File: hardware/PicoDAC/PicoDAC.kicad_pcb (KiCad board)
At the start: 4 copper layers, 29.9 x 82.1 mm, 42 parts, among them CN1 PJ-327A 5JJ, U1 CS43131-CNZR, U2 XIAO-RP2350-DIP, U3 PCA9306DCUR, U4 SN74AXC4T245PWR, U5 XTPS7A2018, U6 TYPEC-955-ARP24, U7 74AHCT1G125GV

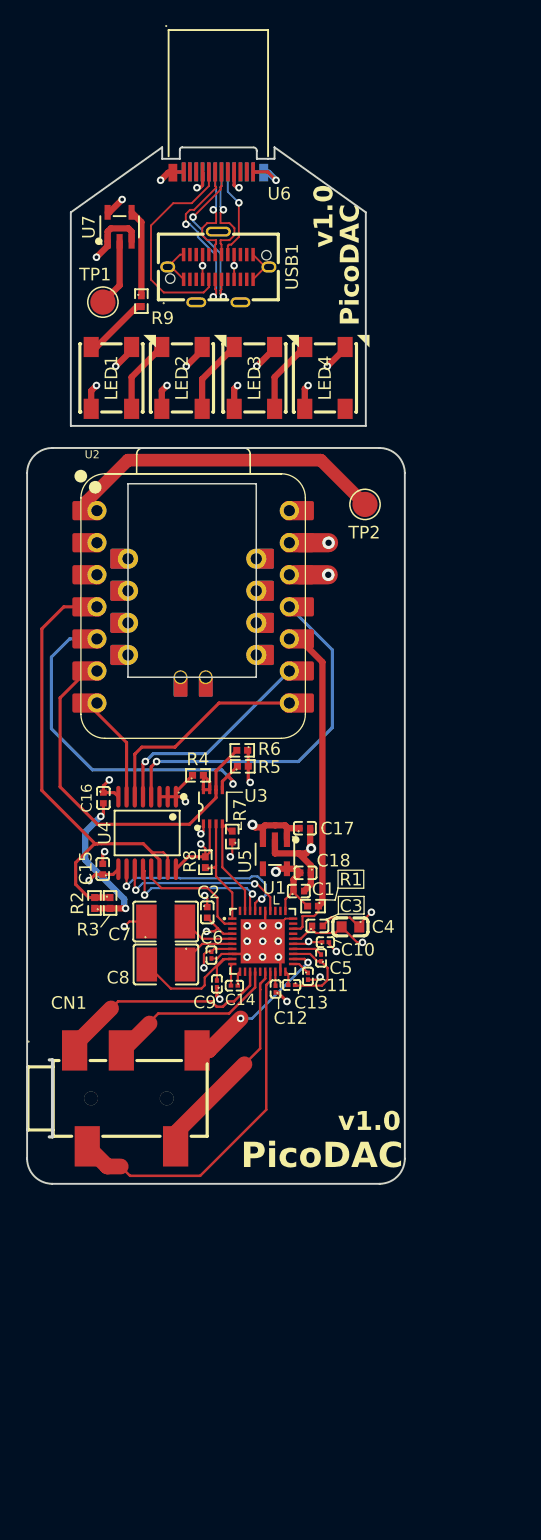
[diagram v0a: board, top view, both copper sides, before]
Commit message: update LEDs position, misc changes to PCBs
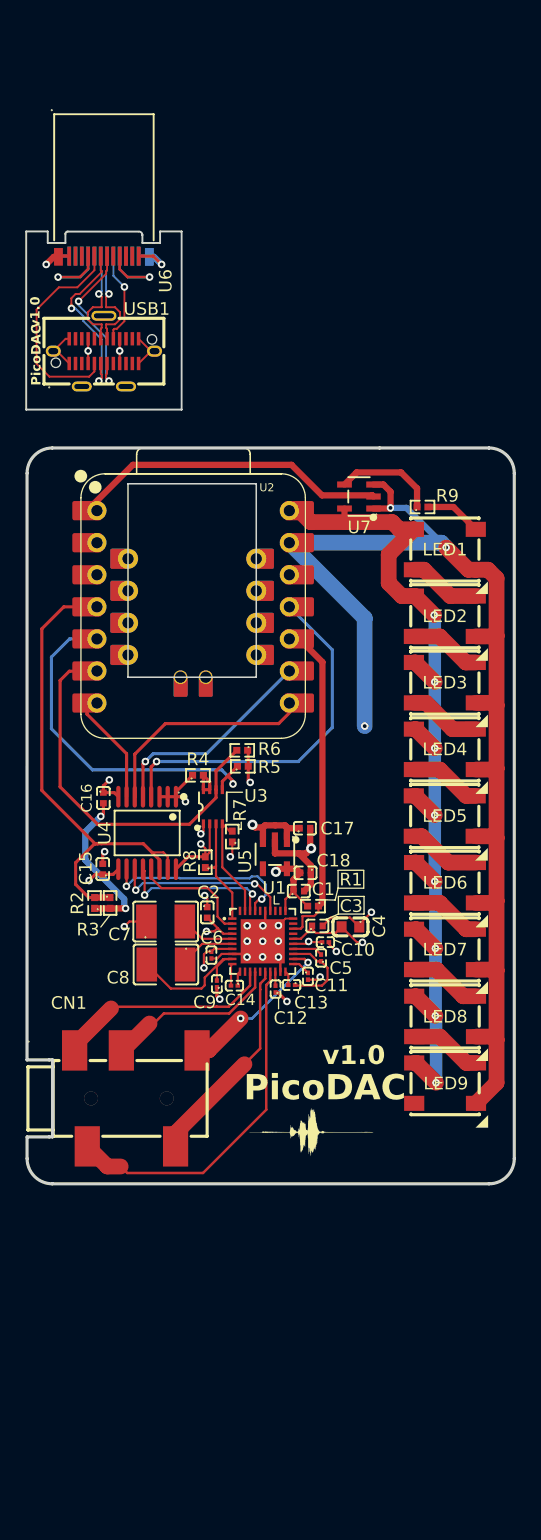
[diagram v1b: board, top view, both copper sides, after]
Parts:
- removed TP1, TP2: TestPoint, TestPoint:TestPoint_Pad_D2.0mm
- added G***: LOGO, LOGO, F.Cu at (153.3, 131.3)
- added LED5: SK6812_C5378720, easyeda2kicad:LED-SMD_4P-L5.4-W5.0_SK6812, F.Cu at (163.9, 106.3)
- added LED6: SK6812_C5378720, easyeda2kicad:LED-SMD_4P-L5.4-W5.0_SK6812, F.Cu at (163.9, 111.6)
- added LED7: SK6812_C5378720, easyeda2kicad:LED-SMD_4P-L5.4-W5.0_SK6812, F.Cu at (163.9, 116.8)
- added LED8: SK6812_C5378720, easyeda2kicad:LED-SMD_4P-L5.4-W5.0_SK6812, F.Cu at (163.9, 122.1)
- added LED9: SK6812_C5378720, easyeda2kicad:LED-SMD_4P-L5.4-W5.0_SK6812, F.Cu at (163.9, 127.4)
- moved LED4 30.9 mm to (163.9, 101.0), turned to 0 degrees
- moved LED1 29.7 mm to (163.9, 85.2), turned to 0 degrees
- moved U7 28.6 mm to (157.1, 81.0), turned to 90 degrees
- moved LED3 28.5 mm to (163.9, 95.7), turned to 0 degrees
- moved LED2 28.1 mm to (163.9, 90.4), turned to 0 degrees
- moved R9 27.6 mm to (162.1, 81.8), turned to 0 degrees
- moved U6 11.3 mm to (136.9, 61.9)
- moved USB1 11.3 mm to (136.9, 69.4)
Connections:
- LED1 pad 1: /USB_GND -> GND
- LED1 pad 3: /USB_VBUS -> VBUS
- LED2 pad 1: /USB_GND -> GND
- LED2 pad 3: /USB_VBUS -> VBUS
- LED3 pad 1: /USB_GND -> GND
- LED3 pad 3: /USB_VBUS -> VBUS
- LED4 pad 1: /USB_GND -> GND
- LED4 pad 3: /USB_VBUS -> VBUS
- LED4 pad 4: unconnected-(LED4-DOUT-Pad4) -> Net-(LED4-DOUT)
- U2 pad 1: /MCU_GP_26 -> /LED_CONTROL
- U7 pad 1: /USB_GND -> GND
- U7 pad 3: /USB_GND -> GND
- U7 pad 5: /USB_VBUS -> VBUS
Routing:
- net GND: track 50.0 -> 146.4 mm, vias 20 -> 22
- net /USB_VBUS: track 102.4 -> 18.6 mm, vias 9 -> 4
- net VBUS: track 0.00 -> 73.8 mm, vias 0 -> 8
- net /MCU_GP_26: track 25.6 -> 0.00 mm
- net /LED_CONTROL: track 5.36 -> 25.3 mm
- net /USB_GND: track 28.4 -> 14.8 mm, vias 7 -> 2
- net Net-(LED7-DOUT): track 0.00 -> 5.78 mm
- net Net-(LED5-DOUT): track 0.00 -> 5.78 mm
- net Net-(LED8-DOUT): track 0.00 -> 5.76 mm
- net Net-(LED6-DOUT): track 0.00 -> 5.76 mm
- net Net-(LED4-DOUT): track 0.00 -> 5.75 mm
- net Net-(U7-Y): track 6.92 -> 8.14 mm
- net /MCU_GP_07: track 29.0 -> 29.8 mm
- net Net-(LED1-DIN): track 5.30 -> 4.52 mm
- net +3.3V: track 88.5 -> 88.8 mm, vias 7 -> 6
- added copper zone on In2.Cu, net /USB_VBUS
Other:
- board size 29.9 x 82.1 mm -> 38.7 x 75.4 mm

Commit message: moved the LEDs a bit down, repositioned LEDs logic level translator and resistor
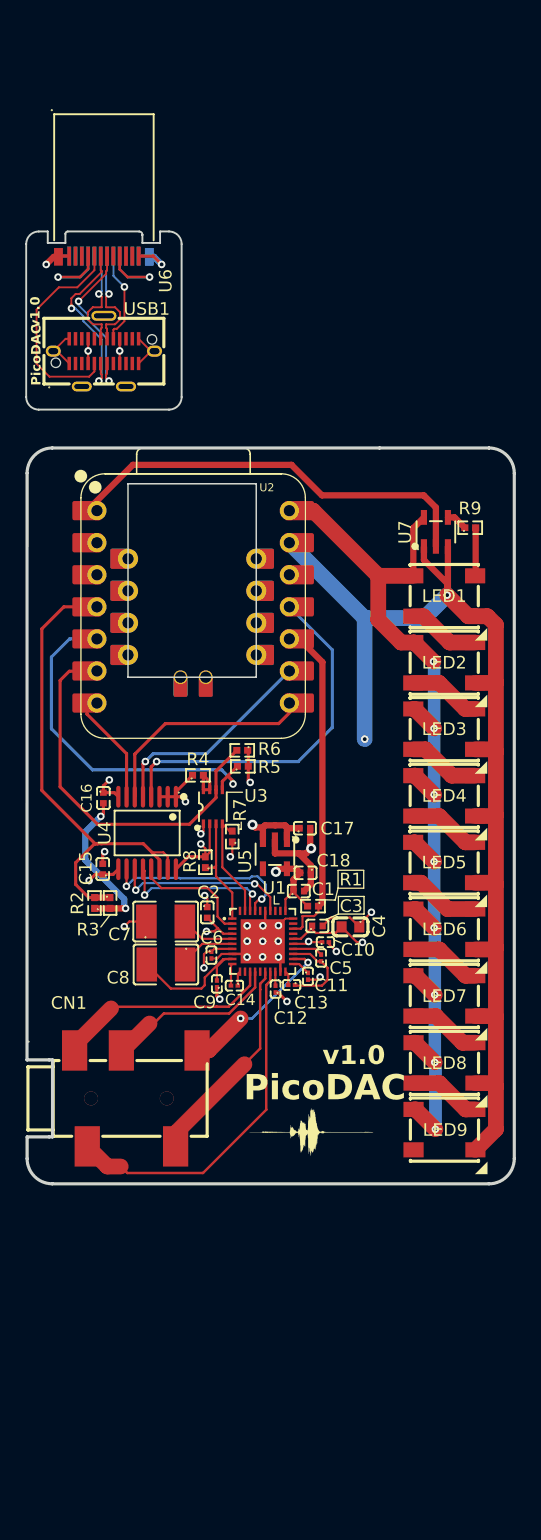
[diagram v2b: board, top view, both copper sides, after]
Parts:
- moved U7 6.71 mm to (163.2, 83.8), turned to 0 degrees
- moved R9 4.12 mm to (165.9, 83.4)
- moved LED1 3.68 mm to (163.8, 88.8)
- moved LED2 3.68 mm to (163.8, 94.1)
- moved LED3 3.68 mm to (163.8, 99.4)
- moved LED4 3.68 mm to (163.8, 104.7)
- moved LED5 3.68 mm to (163.8, 110.0)
- moved LED6 3.68 mm to (163.9, 115.2)
- moved LED7 3.68 mm to (163.9, 120.5)
- moved LED8 3.68 mm to (163.9, 125.8)
- moved LED9 3.68 mm to (163.9, 131.1)
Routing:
- net /LED_CONTROL: track 25.3 -> 33.7 mm
- net Net-(U7-Y): track 8.14 -> 1.68 mm
- net GND: track 146.4 -> 140.5 mm, vias 22 -> 21
- net VBUS: track 73.8 -> 78.6 mm
- net Net-(LED1-DIN): track 4.52 -> 3.83 mm
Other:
- outline, holes or cut-outs redrawn

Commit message: final pcb, rev 1.2
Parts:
- added REF**: MouseBite-Slot_2.0x2.0mm_outset_D0.5mm_P0.85mm_3h, Panelization:MouseBite-Slot_2.0x2.0mm_outset_D0.5mm_P0.85mm_3h, F.Cu at (155.7, 137.4)
- added REF**: MouseBite-Slot_2.0x2.0mm_outset_D0.5mm_P0.85mm_3h, Panelization:MouseBite-Slot_2.0x2.0mm_outset_D0.5mm_P0.85mm_3h, F.Cu at (149.8, 137.4)
- moved U6 89.0 mm to (152.8, 149.6), turned to 0 degrees
- moved USB1 74.3 mm to (152.8, 142.1), turned to 0 degrees
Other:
- board size 38.7 x 75.4 mm -> 38.6 x 74.4 mm

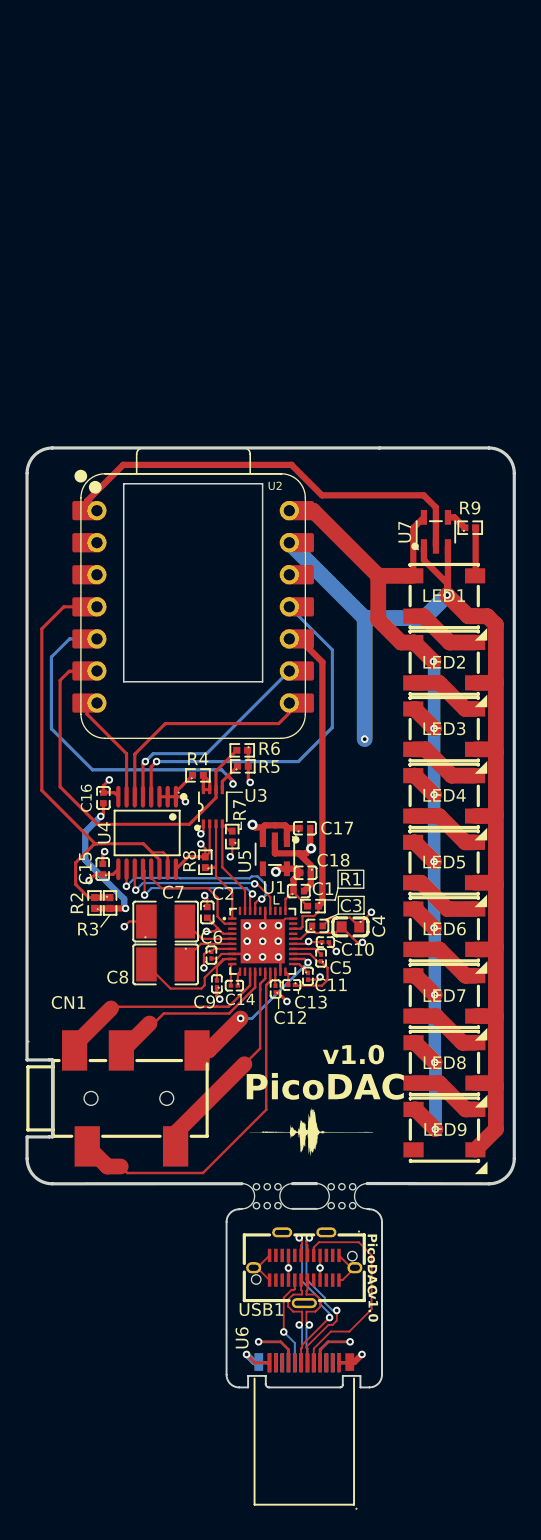
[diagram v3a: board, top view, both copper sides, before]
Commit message: changed components to get economic assembly
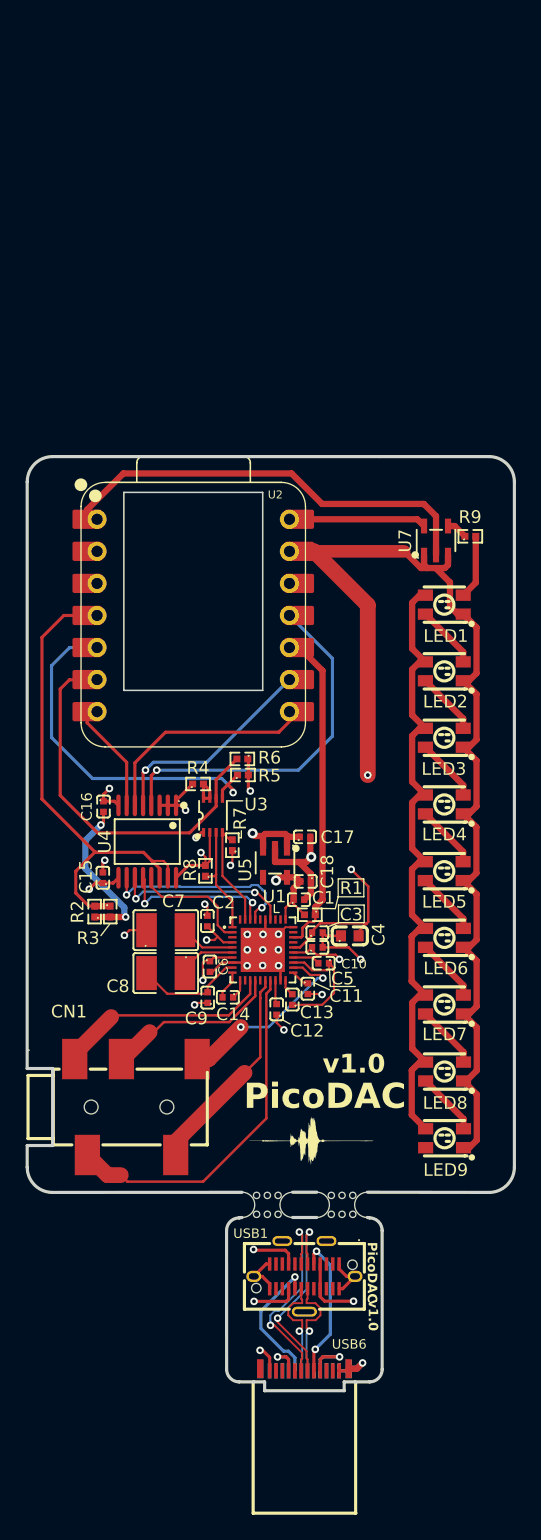
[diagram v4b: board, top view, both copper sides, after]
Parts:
- removed U6: TYPEC-955-ARP24, easyeda2kicad:USB-C-SMD_TYPE-C-24P-GTJB-040
- added USB6: XY-TYPE-C-24PIN-040, easyeda2kicad:USB-C-SMD_XY-TYPE-C-24PIN-040, F.Cu at (152.8, 150.1)
- C10, C11, C12, C13, C14, C5, C6, C9: footprint easyeda2kicad:C0201 -> easyeda2kicad:C0402
- LED1, LED2, LED3, LED4, LED5, LED6, LED7, LED8, LED9: value SK6812_C5378720 -> SK6812_C5142047; footprint easyeda2kicad:LED-SMD_4P-L5.4-W5.0_SK6812 -> easyeda2kicad:LED-SMD_4P-L3.5-W2.8-BR-1
- moved C12 1.61 mm to (150.6, 121.6)
- moved C9 1.30 mm to (145.1, 120.7)
- moved C13 1.15 mm to (151.8, 120.8), turned to 90 degrees
- moved C14 1.06 mm to (146.7, 120.6)
- moved C11 0.99 mm to (153.0, 120.0)
- moved C6 0.92 mm to (145.3, 118.2)
- moved C10 0.76 mm to (153.8, 116.7)
- moved R1 0.73 mm to (153.2, 114.1)
- moved C4 0.72 mm to (156.4, 115.8), turned to 0 degrees
- moved C1 0.68 mm to (152.3, 112.9)
- moved C15 0.68 mm to (136.8, 111.2)
- moved C18 0.68 mm to (152.9, 111.5)
- moved C2 0.68 mm to (145.1, 114.6)
- moved C7 0.68 mm to (141.8, 115.3)
- moved C8 0.68 mm to (141.8, 118.7)
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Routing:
- net VBUS: track 78.6 -> 61.5 mm, vias 8 -> 0
- net /USB_CC1: track 17.1 -> 11.6 mm, vias 0 -> 2
- net /USB_CC2: track 7.39 -> 10.8 mm
- net /USB_VBUS: track 18.6 -> 21.5 mm, vias 4 -> 5
- net /USB_DN1: track 13.3 -> 16.2 mm
- net Net-(U1-FLYC_VCP): track 6.92 -> 9.80 mm
- net Net-(U1--VA): track 11.5 -> 8.63 mm
- net /DAC_HP_DETECT: track 13.7 -> 16.0 mm
- net +1V8: track 34.4 -> 36.7 mm
- net /USB_DP1: track 13.9 -> 15.7 mm
- net +3.3V: track 88.8 -> 90.6 mm
- net /USB_GND: track 14.8 -> 13.4 mm
- net Net-(LED1-DIN): track 3.83 -> 5.07 mm
- net GND: track 140.5 -> 139.4 mm, vias 21 -> 19
- net Net-(U1-VCP_FILT–): track 1.11 -> 1.92 mm
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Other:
- board size 38.6 x 74.4 mm -> 38.6 x 73.3 mm

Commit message: pcb rev 1.4
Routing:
- net GND: track 139.4 -> 130.0 mm
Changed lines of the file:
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@@
 	)
 	(gr_line
+		(start 154.6684 116.676)
+		(end 156.09 116.69)
+		(stroke
+			(width 0.1)
+			(type default)
+		)
+		(layer "F.SilkS")
+	)
+	(gr_line
+		(start 156.09 116.69)
+		(end 156.61 117.36)
+		(stroke
+			(width 0.1)
+			(type default)
+		)
+		(layer "F.SilkS")
+	)
+	(gr_line
 		(start 150.395147 113.2806)
 		(end 150.395147 113.9156)
@@
 	)
 	(segment
-		(start 144.2312 121.0744)
-		(end 144.0728 121.2328)
-		(width 0.175)
+		(start 155.6696 115.8696)
+		(end 156.74 116.94)
+		(width 0.5)
 		(layer "F.Cu")
 		(net 27)
 	)
 	(segment
-		(start 156.279387 116.676)
-		(end 157.229581 117.626194)
-		(width 0.2)
+		(start 144.2312 121.0744)
+		(end 144.0728 121.2328)
+		(width 0.175)
 		(layer "F.Cu")
 		(net 27)
@@
 	)
 	(segment
-		(start 151.279397 115.0786)
-		(end 149.479397 116.8786)
-		(width 0.15)
+		(start 149.679397 114.4686)
+		(end 149.679397 116.6786)
+		(width 0.2)
 		(layer "F.Cu")
 		(net 27)
@@
 	)
 	(segment
-		(start 149.479397 116.8786)
-		(end 149.479397 116.87825)
-		(width 0.15)
+		(start 151.267897 115.0901)
+		(end 149.479397 116.8786)
+		(width 0.175)
 		(layer "F.Cu")
 		(net 27)
@@
 	)
 	(segment
-		(start 149.479397 116.87825)
-		(end 148.249947 115.6488)
-		(width 0.15)
-		(layer "F.Cu")
-		(net 27)
-	)
-	(segment
 		(start 166.419 112.459)
 		(end 165.3492 111.3892)
@@
 	)
 	(segment
-		(start 148.260547 116.8786)
-		(end 148.249947 116.868)
-		(width 0.15)
-		(layer "F.Cu")
-		(net 27)
-	)
-	(segment
 		(start 165.358 100.821643)
 		(end 165.81 100.821643)
@@
 	)
 	(segment
-		(start 151.889397 115.0786)
-		(end 151.279397 115.0786)
-		(width 0.15)
+		(start 148.479397 117.8786)
+		(end 149.479397 116.8786)
+		(width 0.2)
 		(layer "F.Cu")
 		(net 27)
@@
 	)
 	(segment
-		(start 145.492403 118.6168)
-		(end 146.230603 117.8786)
+		(start 151.889397 115.0786)
+		(end 151.877897 115.0901)
 		(width 0.175)
 		(layer "F.Cu")
@@
 	)
 	(segment
-		(start 148.479397 117.8786)
-		(end 149.479397 116.8786)
-		(width 0.2)
-		(layer "F.Cu")
-		(net 27)
-	)
-	(segment
-		(start 149.479397 116.8786)
-		(end 149.479397 115.66395)
-		(width 0.15)
-		(layer "F.Cu")
-		(net 27)
-	)
-	(segment
-		(start 145.2888 118.6168)
-		(end 145.492403 118.6168)
-		(width 0.175)
+		(start 155.6696 115.7672)
+		(end 155.6696 115.8696)
+		(width 0.5)
 		(layer "F.Cu")
 		(net 27)
@@
 	)
 	(segment
-		(start 147.069397 117.8786)
-		(end 148.479397 117.8786)
-		(width 0.2)
-		(layer "F.Cu")
-		(net 27)
-	)
-	(segment
 		(start 165.358 95.558963)
 		(end 165.81 95.558963)
@@
 	)
 	(segment
-		(start 149.679397 114.4686)
-		(end 149.679397 116.6786)
+		(start 145.5708 118.6168)
+		(end 145.2888 118.6168)
 		(width 0.2)
 		(layer "F.Cu")
@@
 	)
 	(segment
+		(start 151.877897 115.0901)
+		(end 151.267897 115.0901)
+		(width 0.175)
+		(layer "F.Cu")
+		(net 27)
+	)
+	(segment
 		(start 152.372953 85.3025)
 		(end 153.538953 85.3025)
@@
 	)
 	(segment
-		(start 154.2184 116.676)
-		(end 156.279387 116.676)
-		(width 0.2)
-		(layer "F.Cu")
-		(net 27)
-	)
-	(segment
 		(start 136.214547 111.5806)
 		(end 135.727747 112.0674)
@@
 	)
 	(segment
-		(start 149.479397 116.88315)
-		(end 148.072147 118.2904)
-		(width 0.15)
-		(layer "F.Cu")
-		(net 27)
-	)
-	(segment
 		(start 136.856947 104.5628)
 		(end 137.327947 104.0918)
@@
 	)
 	(segment
-		(start 149.479397 116.8786)
-		(end 149.479397 118.10235)
-		(width 0.15)
-		(layer "F.Cu")
-		(net 27)
-	)
-	(segment
 		(start 145.086547 114.1696)
 		(end 145.086547 113.4584)
@@
 	)
 	(segment
-		(start 146.230603 117.8786)
-		(end 147.069397 117.8786)
-		(width 0.175)
-		(layer "F.Cu")
-		(net 27)
-	)
-	(segment
 		(start 136.856947 105.1018)
 		(end 137.721247 105.1018)
@@
 	)
 	(segment
-		(start 149.479397 115.66395)
-		(end 149.494547 115.6488)
-		(width 0.15)
-		(layer "F.Cu")
-		(net 27)
-	)
-	(segment
 		(start 166.419 116.0734)
 		(end 166.419 112.459)
@@
 	)
 	(segment
+		(start 156.74 116.94)
+		(end 157.27 116.94)
+		(width 0.5)
+		(layer "F.Cu")
+		(net 27)
+	)
+	(segment
 		(start 154.2184 115.510747)
 		(end 154.222547 115.5066)
@@
 	)
 	(segment
-		(start 150.703147 116.8786)
-		(end 150.713747 116.868)
-		(width 0.15)
-		(layer "F.Cu")
-		(net 27)
-	)
-	(segment
 		(start 166.409 101.872643)
 		(end 165.358 100.821643)
@@
 	)
 	(segment
-		(start 149.479397 116.8786)
-		(end 150.703147 116.8786)
-		(width 0.15)
+		(start 149.8786 116.8786)
+		(end 149.92 116.92)
+		(width 0.2)
 		(layer "F.Cu")
 		(net 27)
@@
 	)
 	(segment
-		(start 149.479397 118.10235)
-		(end 149.469147 118.1126)
-		(width 0.15)
+		(start 147.069397 117.8786)
+		(end 146.309 117.8786)
+		(width 0.2)
 		(layer "F.Cu")
 		(net 27)
@@
 	)
 	(segment
-		(start 150.879397 119.2886)
-		(end 150.879397 118.2786)
-		(width 0.2)
-		(layer "F.Cu")
-		(net 27)
-	)
-	(segment
 		(start 166.4002 110.7902)
 		(end 166.4002 107.147443)
@@
 	)
 	(segment
-		(start 149.479397 116.8786)
-		(end 148.260547 116.8786)
-		(width 0.15)
+		(start 147.069397 117.8786)
+		(end 148.479397 117.8786)
+		(width 0.2)
 		(layer "F.Cu")
 		(net 27)
@@
 	)
 	(segment
+		(start 149.479397 116.8786)
+		(end 149.8786 116.8786)
+		(width 0.2)
+		(layer "F.Cu")
+		(net 27)
+	)
+	(segment
 		(start 164.906 90.275763)
 		(end 164.307 89.676763)
@@
 	)
 	(segment
+		(start 146.309 117.8786)
+		(end 145.5708 118.6168)
+		(width 0.2)
+		(layer "F.Cu")
+		(net 27)
+	)
+	(segment
 		(start 153.292547 111.4518)
 		(end 153.292547 112.3662)
@@
 	)
 	(segment
-		(start 149.479397 116.8786)
-		(end 149.479397 116.88315)
-		(width 0.15)
+		(start 150.879397 119.2886)
+		(end 150.879397 118.2786)
+		(width 0.2)
 		(layer "F.Cu")
 		(net 27)
 	)
 	(via
-		(at 148.237247 118.1253)
+		(at 144.883347 113.2552)
 		(size 0.6)
 		(drill 0.3)
@@
 	)
 	(via
-		(at 144.883347 113.2552)
-		(size 0.6)
-		(drill 0.3)
+		(at 148.25 115.61)
+		(size 0.3)
+		(drill 0.15)
 		(layers "F.Cu" "B.Cu")
 		(net 27)
 	)
 	(via
-		(at 151.1512 123.2168)
-		(size 0.6)
-		(drill 0.3)
+		(at 149.479397 116.8786)
+		(size 0.3)
+		(drill 0.15)
 		(layers "F.Cu" "B.Cu")
 		(net 27)
 	)
 	(via
-		(at 148.249947 115.6488)
+		(at 151.1512 123.2168)
 		(size 0.6)
 		(drill 0.3)
@@
 	)
 	(via
-		(at 148.249947 116.868)
-		(size 0.6)
-		(drill 0.3)
+		(at 148.229397 118.1286)
+		(size 0.3)
+		(drill 0.15)
 		(layers "F.Cu" "B.Cu")
 		(net 27)
@@
 	)
 	(via
-		(at 149.494547 115.6488)
-		(size 0.6)
-		(drill 0.3)
+		(at 148.229397 116.8786)
+		(size 0.3)
+		(drill 0.15)
+		(layers "F.Cu" "B.Cu")
+		(net 27)
+	)
+	(via
+		(at 149.479397 115.6286)
+		(size 0.3)
+		(drill 0.15)
 		(layers "F.Cu" "B.Cu")
 		(net 27)
@@
 	)
 	(via
-		(at 144.180414 107.986618)
+		(at 157.27 116.94)
 		(size 0.6)
 		(drill 0.3)
@@
 	)
 	(via
-		(at 150.724172 115.633825)
+		(at 144.180414 107.986618)
 		(size 0.6)
 		(drill 0.3)
@@
 	)
 	(via
-		(at 150.713747 116.868)
-		(size 0.6)
-		(drill 0.3)
+		(at 150.729397 115.6286)
+		(size 0.3)
+		(drill 0.15)
 		(layers "F.Cu" "B.Cu")
 		(net 27)
 	)
 	(via
-		(at 144.0728 121.2328)
-		(size 0.6)
-		(drill 0.3)
+		(at 149.479397 118.1286)
+		(size 0.3)
+		(drill 0.15)
 		(layers "F.Cu" "B.Cu")
 		(net 27)
 	)
 	(via
-		(at 157.229581 117.626194)
-		(size 0.6)
-		(drill 0.3)
+		(at 150.729397 116.8786)
+		(size 0.3)
+		(drill 0.15)
 		(layers "F.Cu" "B.Cu")
 		(net 27)
 	)
 	(via
-		(at 149.469147 118.1126)
+		(at 144.0728 121.2328)
 		(size 0.6)
 		(drill 0.3)
@@
 	)
 	(via
-		(at 149.479397 116.87825)
-		(size 0.6)
-		(drill 0.3)
+		(at 150.729397 118.1286)
+		(size 0.3)
+		(drill 0.15)
 		(layers "F.Cu" "B.Cu")
 		(net 27)
@@
 		(layers "F.Cu" "B.Cu")
 		(net 27)
-	)
-	(via
-		(at 150.726272 118.125475)
-		(size 0.6)
-		(drill 0.3)
-		(layers "F.Cu" "B.Cu")
-		(net 27)
